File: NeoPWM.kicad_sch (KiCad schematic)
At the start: 0 parts

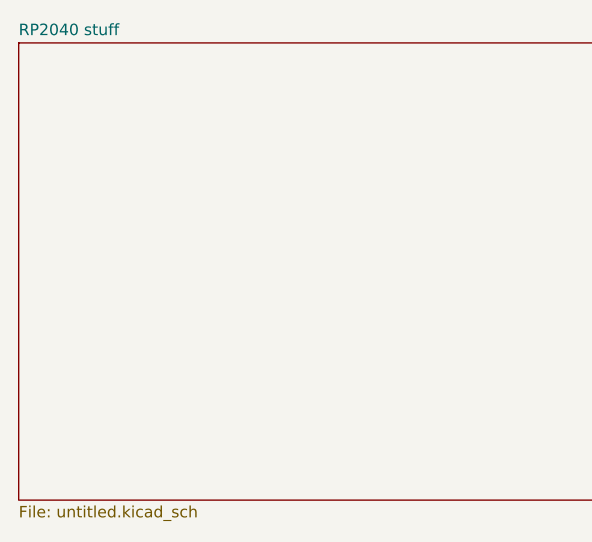
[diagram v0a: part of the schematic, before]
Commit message: Rename "RP2040 stuff" to "RP2040 Circuitry" in schematic and project files
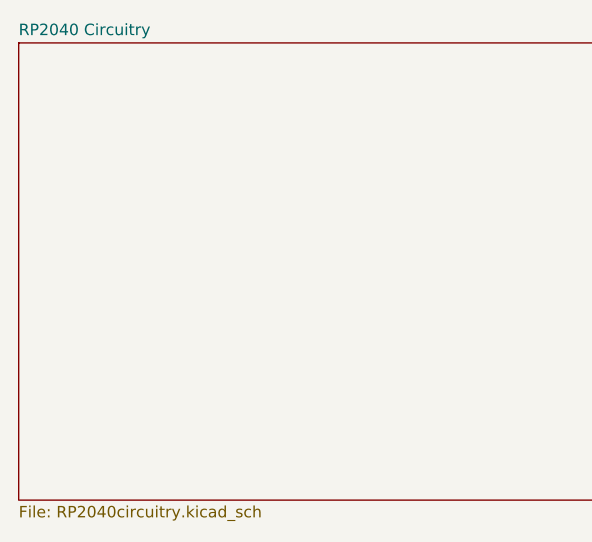
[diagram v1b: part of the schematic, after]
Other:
- sheet RP2040 stuff renamed RP2040 Circuitry
- sheet RP2040 Circuitry: file untitled.kicad_sch -> RP2040circuitry.kicad_sch
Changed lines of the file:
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@@
 			(color 0 0 0 0.0000)
 		)
-		(property "Sheetname" "RP2040 stuff"
+		(property "Sheetname" "RP2040 Circuitry"
 			(at 31.75 28.4984 0)
 			(effects
@@
 			)
 		)
-		(property "Sheetfile" "untitled.kicad_sch"
+		(property "Sheetfile" "RP2040circuitry.kicad_sch"
 			(at 31.75 80.5946 0)
 			(effects

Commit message: Power + Optocoupler
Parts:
- added J2: PWM Input, Connector:FanPinHeader_1x03_P2.54mm_Vertical, symbol Connector:Conn_01x03_Pin
- added R5: 470, symbol Device:R
- added R6: 4.7k, symbol Device:R
- added U4: LTV-357T, Package_DIP:DIP-4_W7.62mm, symbol Isolator:LTV-357T
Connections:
- new net: R5.2, U4.1
- new net +3V3: R6.1
- new net GND: U4.3
- new net PWM 5v: J2.2 (Pin_2)
- new net PWM GND: J2.1 (Pin_1), U4.2
- new net PWM Signal: J2.3 (Pin_3), R5.1
- new net PWM Signal GPIO: R6.2, U4.4
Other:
- note added: "Control Hub level logic"

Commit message: 3D Models
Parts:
- added J3: NeoPixel Connector, 691137710003:CONN3_WR-TBL-1377_WRE, symbol Connector:Conn_01x03_Pin
- R5, R6: footprint (none) -> Resistor_SMD:R_0402_1005Metric
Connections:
- net NeoPixel 5v: now also J3.2 (Pin_2)
- net NeoPixel GND: now also J3.3 (Pin_3)
- net NeoPixel Signal: now also J3.1 (Pin_1)
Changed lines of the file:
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@@
+	(wire
+		(pts
+			(xy 248.92 43.18) (xy 252.73 43.18)
+		)
+		(stroke
+			(width 0)
+			(type default)
+		)
+	)
 	(wire
 		(pts
@@
 		(pts
 			(xy 200.66 25.4) (xy 200.66 29.21)
+		)
+		(stroke
+			(width 0)
+			(type default)
+		)
+	)
+	(wire
+		(pts
+			(xy 248.92 40.64) (xy 252.73 40.64)
+		)
+		(stroke
+			(width 0)
+			(type default)
+		)
+	)
+	(wire
+		(pts
+			(xy 248.92 38.1) (xy 252.73 38.1)
 		)
 		(stroke
@@
 	)
 	(symbol
+		(lib_id "Connector:Conn_01x03_Pin")
+		(at 243.84 40.64 0)
+		(unit 1)
+		(exclude_from_sim no)
+		(in_bom yes)
+		(on_board yes)
+		(dnp no)
+		(fields_autoplaced yes)
+		(property "Reference" "J3"
+			(at 244.475 33.02 0)
+			(effects
+				(font
+					(size 1.27 1.27)
+				)
+			)
+		)
+		(property "Value" "NeoPixel Connector"
+			(at 244.475 35.56 0)
+			(effects
+				(font
+					(size 1.27 1.27)
+				)
+			)
+		)
+		(property "Footprint" "691137710003:CONN3_WR-TBL-1377_WRE"
+			(at 243.84 40.64 0)
+			(effects
+				(font
+					(size 1.27 1.27)
+				)
+				(hide yes)
+			)
+		)
+		(property "Datasheet" "~"
+			(at 243.84 40.64 0)
+			(effects
+				(font
+					(size 1.27 1.27)
+				)
+				(hide yes)
+			)
+		)
+		(property "Description" "Generic connector, single row, 01x03, script generated"
+			(at 243.84 40.64 0)
+			(effects
+				(font
+					(size 1.27 1.27)
+				)
+				(hide yes)
+			)
+		)
+		(pin "1"
+		)
+		(pin "3"
+		)
+		(pin "2"
+		)
+		(instances
+			(project ""
+				(path "/5f4f8df1-f390-4405-b7ce-064ebaa7e775"
+					(reference "J3")
+					(unit 1)
+				)
+			)
+		)
+	)
+	(symbol
 		(lib_id "power:+3V3")
 		(at 200.66 25.4 0)
@@
 			)
 		)
-		(property "Footprint" ""
+		(property "Footprint" "Resistor_SMD:R_0402_1005Metric"
 			(at 198.882 33.02 90)
 			(effects
@@
 			)
 		)
-		(property "Footprint" ""
+		(property "Footprint" "Resistor_SMD:R_0402_1005Metric"
 			(at 165.1 41.148 90)
 			(effects

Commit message: Finished schematic
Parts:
- J2: footprint Connector:FanPinHeader_1x03_P2.54mm_Vertical -> Connector_PinHeader_2.54mm:PinHeader_1x03_P2.54mm_Horizontal
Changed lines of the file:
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@@
 			)
 		)
-		(property "Footprint" "Connector:FanPinHeader_1x03_P2.54mm_Vertical"
+		(property "Footprint" "Connector_PinHeader_2.54mm:PinHeader_1x03_P2.54mm_Horizontal"
 			(at 121.92 41.91 0)
 			(effects

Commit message: ahaha
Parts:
- added H1, H2, H3, H4: MountingHole_Pad, MountingHole:MountingHole_2.2mm_M2_Pad, symbol Mechanical:MountingHole_Pad
- U4: footprint Package_DIP:DIP-4_W7.62mm -> LTV-217-B-G:SOIC127P700X210-4N
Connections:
- net NeoPixel 5v is gone; now on net NeoPixel Signal: J3.2 (Pin_2)
- net NeoPixel GND is gone; now on net GND: J3.3 (Pin_3)
- net GND: now also H1.1, H2.1, H3.1, H4.1
- net NeoPixel Signal: no longer J3.1 (Pin_1)
- new net VBUS: J3.1 (Pin_1)

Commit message: he
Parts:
- J3: footprint 691137710003:CONN3_WR-TBL-1377_WRE -> Connector_JST:JST_PH_S3B-PH-K_1x03_P2.00mm_Horizontal
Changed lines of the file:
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@@
 			)
 		)
-		(property "Footprint" "691137710003:CONN3_WR-TBL-1377_WRE"
+		(property "Footprint" "Connector_JST:JST_PH_S3B-PH-K_1x03_P2.00mm_Horizontal"
 			(at 243.84 40.64 0)
 			(effects
